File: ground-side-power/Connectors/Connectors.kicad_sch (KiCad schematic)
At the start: 12 parts, among them J15 To Router, J16 To RLCS, J17 To DAQ Laptop, J18 Conn_01x02_Female, J19 Conn_01x02_Female, J20 To Ethernet, J21 To 5V M12, J22 To DAQ, J23 Extra M12, J24 Extra M12, J25 Extra M12, M2 Fan_PC_Chassis

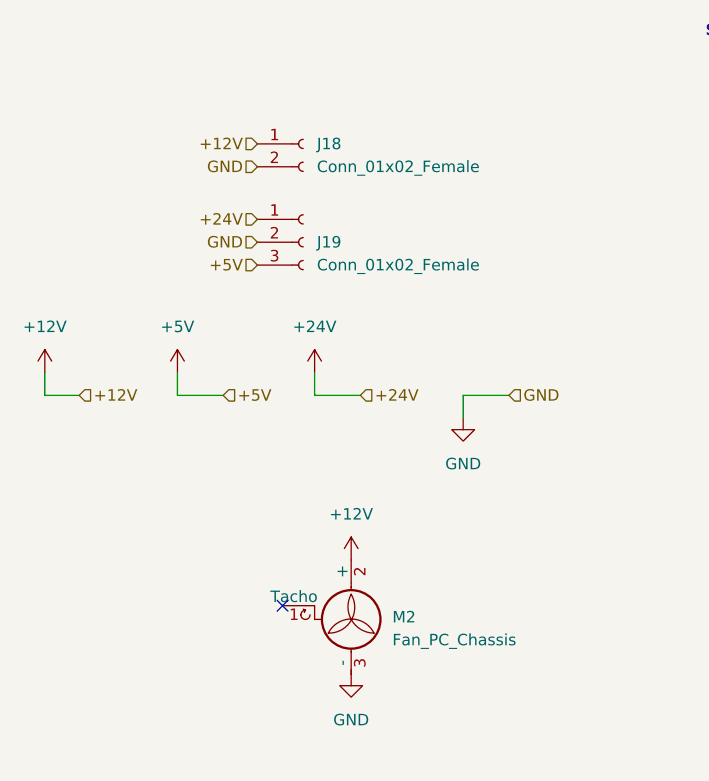
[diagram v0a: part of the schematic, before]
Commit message: resolved issues from testing
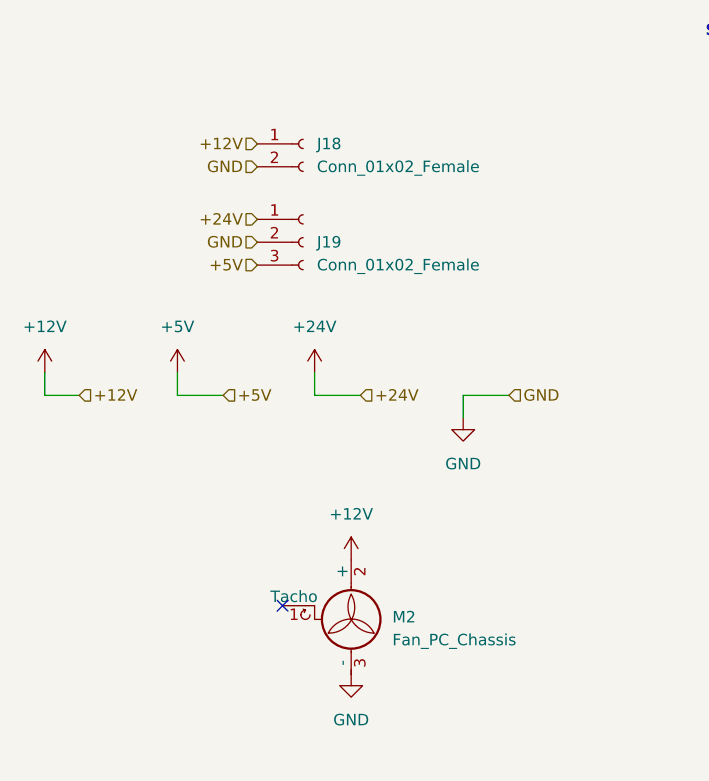
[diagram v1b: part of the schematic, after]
